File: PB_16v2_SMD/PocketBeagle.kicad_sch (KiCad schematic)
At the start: 2 parts, among them U1 POCKETBEAGLE-SC-569

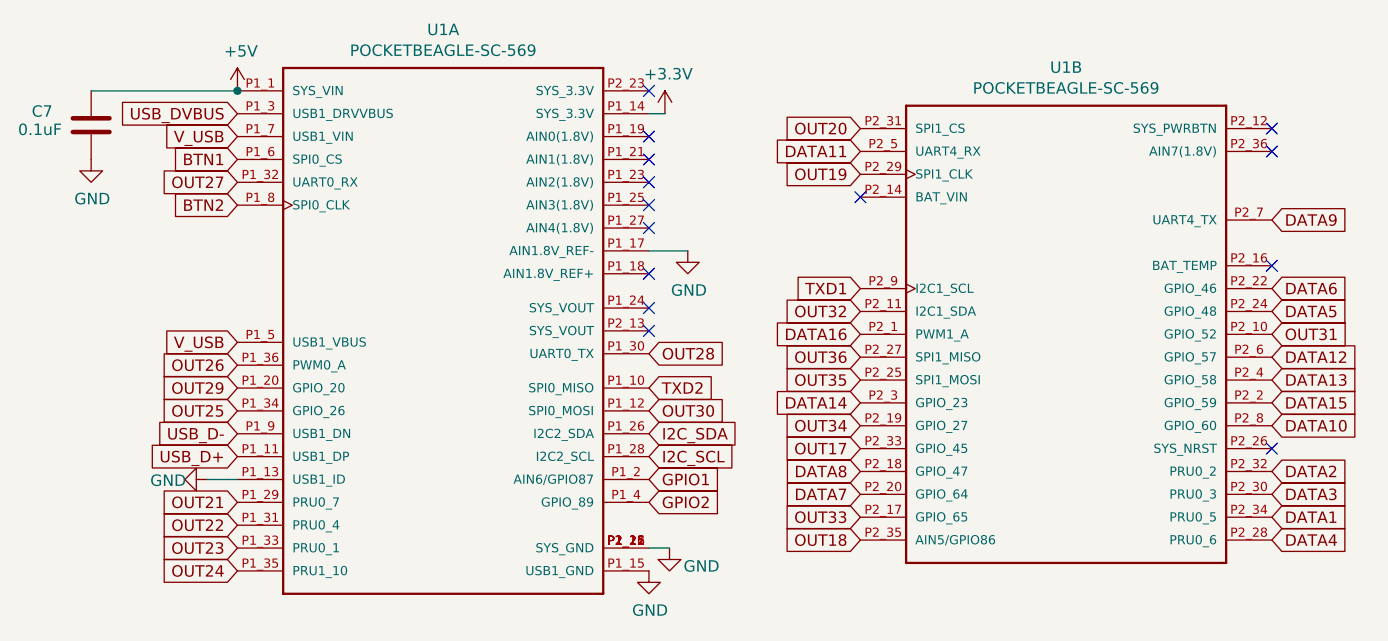
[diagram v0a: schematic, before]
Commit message: Switched to SMD resistors, need to fix BOM
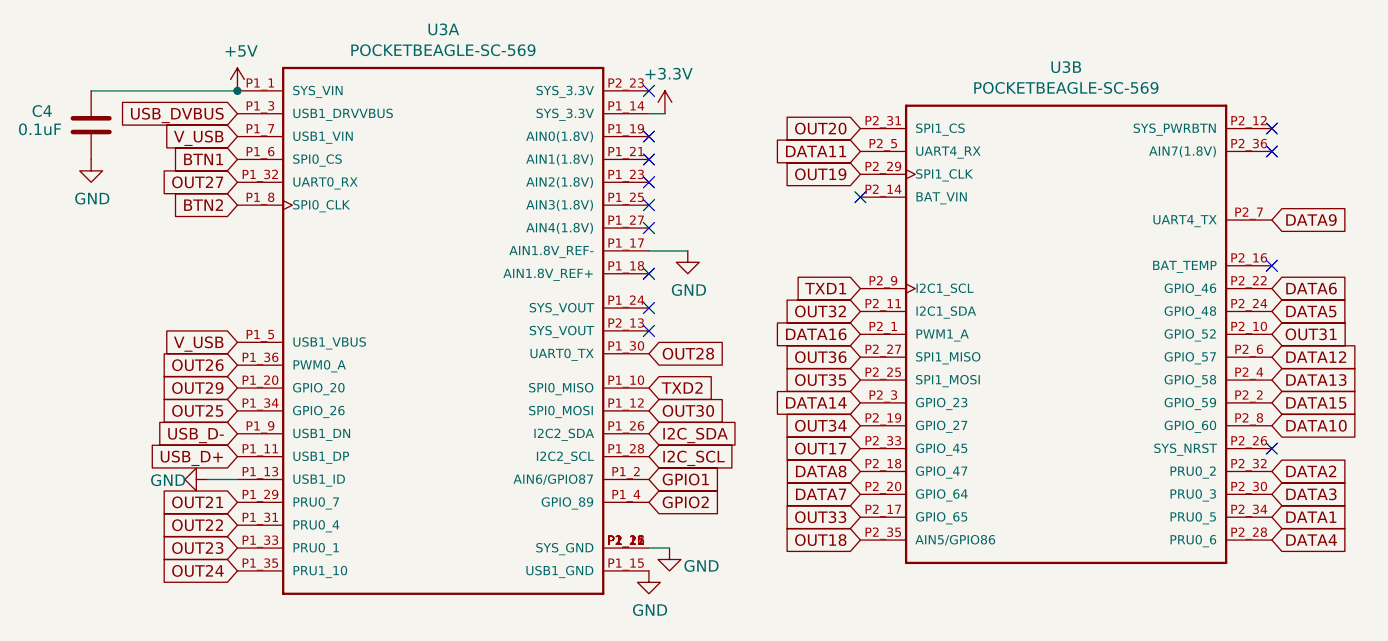
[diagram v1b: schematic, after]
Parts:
- C4: renamed from C7; footprint Capacitor_SMD:C_0805_2012Metric_Pad1.15x1.40mm_HandSolder -> Capacitor_SMD:C_0805_2012Metric_Pad1.18x1.45mm_HandSolder
- renumbered U1 to U3
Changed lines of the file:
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@@
   (title_block
     (title "PB 16")
-    (date "2020-08-11")
-    (rev "v2")
+    (date "2022-05-26")
+    (rev "v2.1")
     (company "Scott Hanson")
   )
@@
   (symbol (lib_id "POCKETBEAGLE:POCKETBEAGLE-SC-569") (at 178.308 92.837 0) (unit 2)
     (in_bom yes) (on_board yes)
-    (property "Reference" "U1" (id 0) (at 178.308 63.1952 0))
+    (property "Reference" "U3" (id 0) (at 178.308 63.1952 0))
     (property "Value" "POCKETBEAGLE-SC-569" (id 1) (at 178.308 65.5066 0))
     (property "Footprint" "POCKETBEAGLE:BEAGLE_POCKETBEAGLE-SC-569" (id 2) (at 178.308 92.837 0)
@@
   (symbol (lib_id "POCKETBEAGLE:POCKETBEAGLE-SC-569") (at 109.093 91.186 0) (unit 1)
     (in_bom yes) (on_board yes)
-    (property "Reference" "U1" (id 0) (at 109.093 59.0042 0))
+    (property "Reference" "U3" (id 0) (at 109.093 59.0042 0))
     (property "Value" "POCKETBEAGLE-SC-569" (id 1) (at 109.093 61.3156 0))
     (property "Footprint" "POCKETBEAGLE:BEAGLE_POCKETBEAGLE-SC-569" (id 2) (at 109.093 91.186 0)
@@
   (symbol (lib_id "power:+5V") (at 86.233 65.786 0) (unit 1)
     (in_bom yes) (on_board yes)
-    (property "Reference" "#PWR0127" (id 0) (at 86.233 69.596 0)
+    (property "Reference" "#PWR040" (id 0) (at 86.233 69.596 0)
       (effects (font (size 1.27 1.27)) hide)
     )
@@
   (symbol (lib_id "power:GND") (at 131.953 119.126 0) (unit 1)
     (in_bom yes) (on_board yes)
-    (property "Reference" "#PWR0128" (id 0) (at 131.953 125.476 0)
+    (property "Reference" "#PWR041" (id 0) (at 131.953 125.476 0)
       (effects (font (size 1.27 1.27)) hide)
     )
@@
   (symbol (lib_id "power:GND") (at 134.239 116.586 0) (unit 1)
     (in_bom yes) (on_board yes)
-    (property "Reference" "#PWR0129" (id 0) (at 134.239 122.936 0)
+    (property "Reference" "#PWR043" (id 0) (at 134.239 122.936 0)
       (effects (font (size 1.27 1.27)) hide)
     )
@@
   (symbol (lib_id "power:GND") (at 136.271 83.566 0) (unit 1)
     (in_bom yes) (on_board yes)
-    (property "Reference" "#PWR0130" (id 0) (at 136.271 89.916 0)
+    (property "Reference" "#PWR044" (id 0) (at 136.271 89.916 0)
       (effects (font (size 1.27 1.27)) hide)
     )
@@
   (symbol (lib_id "power:GND") (at 82.931 108.966 270) (unit 1)
     (in_bom yes) (on_board yes)
-    (property "Reference" "#PWR0131" (id 0) (at 76.581 108.966 0)
+    (property "Reference" "#PWR039" (id 0) (at 76.581 108.966 0)
       (effects (font (size 1.27 1.27)) hide)
     )
@@
   (symbol (lib_id "Device:C") (at 69.977 69.596 0) (unit 1)
     (in_bom yes) (on_board yes)
-    (property "Reference" "C7" (id 0) (at 63.373 68.072 0)
+    (property "Reference" "C4" (id 0) (at 63.373 68.072 0)
       (effects (font (size 1.27 1.27)) (justify left))
     )
@@
       (effects (font (size 1.27 1.27)) (justify left))
     )
-    (property "Footprint" "Capacitor_SMD:C_0805_2012Metric_Pad1.15x1.40mm_HandSolder" (id 2) (at 70.9422 73.406 0)
+    (property "Footprint" "Capacitor_SMD:C_0805_2012Metric_Pad1.18x1.45mm_HandSolder" (id 2) (at 70.9422 73.406 0)
       (effects (font (size 1.27 1.27)) hide)
     )
@@
   (symbol (lib_id "power:GND") (at 69.977 73.406 0) (unit 1)
     (in_bom yes) (on_board yes)
-    (property "Reference" "#PWR0132" (id 0) (at 69.977 79.756 0)
+    (property "Reference" "#PWR038" (id 0) (at 69.977 79.756 0)
       (effects (font (size 1.27 1.27)) hide)
     )
@@
   (symbol (lib_id "power:+3.3V") (at 133.731 68.326 0) (unit 1)
     (in_bom yes) (on_board yes)
-    (property "Reference" "#PWR0133" (id 0) (at 133.731 72.136 0)
-      (effects (font (size 1.27 1.27)) hide)
-    )
+    (property "Reference" "#PWR042" (id 0) (at 133.731 72.136 0)
+      (effects (font (size 1.27 1.27)) hide)
+    )

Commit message: Added Dual Port Expansion
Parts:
- C4: footprint Capacitor_SMD:C_0805_2012Metric_Pad1.18x1.45mm_HandSolder -> Capacitor_SMD:C_0603_1608Metric_Pad1.08x0.95mm_HandSolder
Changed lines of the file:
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@@
       (effects (font (size 1.27 1.27)) (justify left))
     )
-    (property "Footprint" "Capacitor_SMD:C_0805_2012Metric_Pad1.18x1.45mm_HandSolder" (id 2) (at 70.9422 73.406 0)
+    (property "Footprint" "Capacitor_SMD:C_0603_1608Metric_Pad1.08x0.95mm_HandSolder" (id 2) (at 70.9422 73.406 0)
       (effects (font (size 1.27 1.27)) hide)
     )

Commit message: switched Resistors and Capacitors to 603 packages
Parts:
- C4: Digi-Key_PN 1276-1007-1-ND -> 1276-1935-2-ND; LCSC C49678 -> C14663; MPN CL21F104ZBCNNNC -> CL10B104KB8NNWC
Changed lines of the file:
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@@
   (title_block
     (title "PB 16")
-    (date "2022-05-26")
-    (rev "v2.1")
+    (date "2022-06-05")
+    (rev "v2.2")
     (company "Scott Hanson")
   )
@@
       (effects (font (size 1.27 1.27)) hide)
     )
-    (property "Digi-Key_PN" "1276-1007-1-ND" (id 4) (at 69.977 69.596 0)
-      (effects (font (size 1.27 1.27)) hide)
-    )
-    (property "MPN" "CL21F104ZBCNNNC" (id 5) (at 69.977 69.596 0)
-      (effects (font (size 1.27 1.27)) hide)
-    )
-    (property "LCSC" "C49678" (id 6) (at 69.977 69.596 0)
-      (effects (font (size 1.27 1.27)) hide)
-    )
+    (property "Digi-Key_PN" "1276-1935-2-ND" (id 4) (at 69.977 69.596 0)
+      (effects (font (size 1.27 1.27)) hide)
+    )
+    (property "MPN" "CL10B104KB8NNWC" (id 5) (at 69.977 69.596 0)
+      (effects (font (size 1.27 1.27)) hide)
+    )
+    (property "LCSC" "C14663" (id 6) (at 69.977 69.596 0)
+      (effects (font (size 1.27 1.27)) hide)
+    )

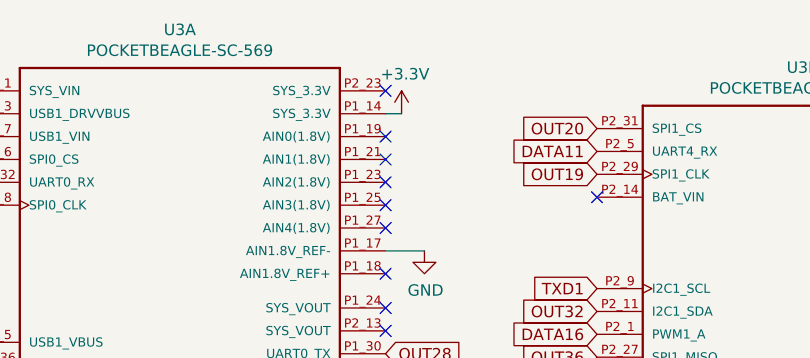
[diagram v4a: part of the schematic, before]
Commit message: v2.3 ---- * 2026-02-09 * Switched to TSSOP-20 for U4 & U5. * Switched to 603 Resistors for Pixel Outputs. * Switched Pixel Outputs to Dual 3.5mm/3.81mm Pads. * Switched Expansion Header to 24pin Falcon V4 pinout. * Removed Top Solder pour.
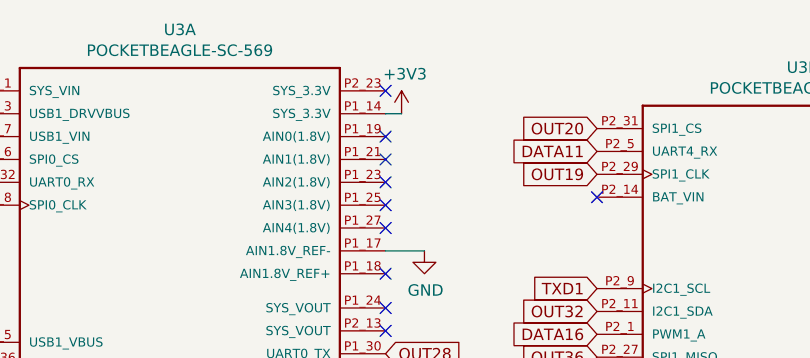
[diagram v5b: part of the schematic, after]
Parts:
- C4: footprint Capacitor_SMD:C_0603_1608Metric_Pad1.08x0.95mm_HandSolder -> Capacitor_SMD:C_0603_1608Metric
